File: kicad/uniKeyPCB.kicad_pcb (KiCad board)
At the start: 2 copper layers, 84 x 84 mm, 136 parts, among them J1 Conn_01x03_Socket, J10 Conn_01x02_Socket, J2 Conn_01x03_Socket, J3 Conn_01x02_Socket, J4 Conn_01x02_Socket, J5 Conn_01x03_Socket, J6 Conn_01x03_Socket, J9 Conn_01x02_Socket, SW1 SW_CHOC_HS, SW2 SW_MX_HS

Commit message: wip
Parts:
- removed the D1 at (75.5, 130.6)
- removed the D1 at (118.6, 130.6)
- removed the D1 at (75.5, 87.6)
- removed the D1 at (75.5, 109.1)
- removed the D1 at (118.6, 66.1)
- removed the D1 at (75.5, 66.1)
- removed the D1 at (118.6, 109.0)
- removed the D2 at (85.8, 65.4)
- removed the D2 at (128.8, 129.8)
- removed the D2 at (128.8, 65.4)
- removed the D2 at (85.8, 129.8)
- removed the D2 at (128.8, 108.3)
- removed the D2 at (128.8, 86.9)
- removed the D2 at (85.8, 108.3)
- removed the J1 at (119.2, 54.2)
- removed the J1 at (119.2, 118.6)
- removed the J1 at (76.2, 54.2)
- removed the J1 at (76.2, 75.7)
- removed the J1 at (119.2, 97.1)
- removed the J1 at (76.2, 97.1)
- removed the J1 at (76.2, 118.6)
- removed the J10 at (63.0, 136.0)
- removed the J10 at (106.0, 114.5)
- removed the J10 at (106.0, 71.5)
- removed the J10 at (63.0, 93.0)
- removed the J10 at (63.0, 114.5)
- removed the J10 at (106.0, 135.9)
- removed the J10 at (63.0, 71.5)
- removed the J2 at (76.3, 71.5)
- removed the J2 at (76.3, 114.5)
- removed the J2 at (119.3, 136.0)
- removed the J2 at (76.3, 136.0)
- removed the J2 at (119.3, 71.5)
- removed the J2 at (76.3, 93.0)
- removed the J2 at (119.3, 114.5)
- removed the J3 at (142.1, 71.4)
- removed the J3 at (99.1, 114.4)
- removed the J3 at (142.1, 135.9)
- removed the J3 at (99.1, 135.9)
- removed the J3 at (142.1, 114.4)
- removed the J3 at (99.1, 71.4)
- removed the J3 at (142.1, 92.9)
- removed the J4 at (142.1, 97.3)
- removed the J4 at (142.1, 118.8)
- removed the J4 at (99.1, 54.3)
- removed the J4 at (142.1, 75.8)
- removed the J4 at (99.1, 118.8)
- removed the J4 at (142.1, 54.3)
- removed the J4 at (99.1, 97.3)
- removed the J5 at (128.8, 114.5)
- removed the J5 at (85.8, 71.6)
- removed the J5 at (85.8, 136.0)
- removed the J5 at (85.8, 114.5)
- removed the J5 at (128.8, 136.0)
- removed the J5 at (128.8, 93.0)
- removed the J5 at (128.8, 71.5)
- removed the J6 at (85.9, 118.6)
- removed the J6 at (85.9, 54.1)
- removed the J6 at (128.9, 54.1)
- removed the J6 at (128.9, 118.6)
- removed the J6 at (128.9, 75.6)
- removed the J6 at (128.9, 97.1)
- removed the J6 at (85.9, 97.1)
- removed the J9 at (63.0, 118.8)
- removed the J9 at (106.0, 97.3)
- removed the J9 at (106.0, 54.3)
- removed the J9 at (63.0, 97.3)
- removed the J9 at (63.0, 75.8)
- removed the J9 at (106.0, 118.8)
- removed the J9 at (63.0, 54.3)
- removed the LED1 at (113.3, 122.3)
- removed the LED1 at (70.3, 100.8)
- removed the LED1 at (113.3, 57.8)
- removed the LED1 at (70.3, 79.3)
- removed the LED1 at (113.3, 100.8)
- removed the LED1 at (70.3, 57.8)
- removed the LED1 at (70.3, 122.3)
- removed the LED2 at (134.8, 89.5)
- removed the LED2 at (134.8, 110.9)
- removed the LED2 at (91.8, 110.9)
- removed the LED2 at (91.8, 132.4)
- removed the LED2 at (91.8, 68.0)
- removed the LED2 at (134.8, 68.0)
- removed the LED2 at (134.8, 132.4)
- removed the SW1 at (70.3, 62.9)
- removed the SW1 at (113.3, 127.3)
- removed the SW1 at (113.3, 105.8)
- removed the SW1 at (70.3, 105.9)
- removed the SW1 at (113.3, 62.9)
- removed the SW1 at (70.3, 127.4)
- removed the SW1 at (70.3, 84.4)
- removed the SW2 at (91.8, 62.9)
- removed the SW2 at (134.8, 127.3)
- removed the SW2 at (134.8, 105.8)
- removed the SW2 at (134.8, 62.9)
- removed the SW2 at (91.8, 127.4)
- removed the SW2 at (134.8, 84.4)
- removed the SW2 at (91.8, 105.9)
- removed the mouse-bite-2mm-slot at (113.3, 95.1)
- removed the mouse-bite-2mm-slot at (81.1, 62.9)
- removed the mouse-bite-2mm-slot at (91.8, 95.2)
- removed the mouse-bite-2mm-slot at (70.3, 95.2)
- removed the mouse-bite-2mm-slot at (102.6, 62.9)
- removed the mouse-bite-2mm-slot at (102.6, 127.3)
- removed the mouse-bite-2mm-slot at (102.6, 105.8)
- removed the mouse-bite-2mm-slot at (70.3, 73.7)
- removed the mouse-bite-2mm-slot at (124.1, 127.3)
- removed the mouse-bite-2mm-slot at (124.1, 105.8)
- removed the mouse-bite-2mm-slot at (91.8, 116.6)
- removed the mouse-bite-2mm-slot at (134.8, 73.6)
- removed the mouse-bite-2mm-slot at (113.3, 116.6)
- removed the mouse-bite-2mm-slot at (81.1, 127.4)
- removed the mouse-bite-2mm-slot at (81.1, 84.4)
- removed the mouse-bite-2mm-slot at (134.8, 116.6)
- removed the mouse-bite-2mm-slot at (134.8, 95.1)
- removed the mouse-bite-2mm-slot at (124.1, 62.9)
- removed the mouse-bite-2mm-slot at (81.1, 105.9)
- removed the mouse-bite-2mm-slot at (70.3, 116.6)
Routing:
- net VCC: track 338.8 -> 42.3 mm
- net col0: track 262.1 -> 32.8 mm
- net col1: track 243.6 -> 30.7 mm
- net LED0_out: track 174.1 -> 21.8 mm
- net row1: track 148.0 -> 18.5 mm
- net row0: track 125.2 -> 15.6 mm
- net LED1_in: track 45.0 -> 5.63 mm
- net Net-(D2-A): track 44.6 -> 5.58 mm
- net LED0_in: track 41.0 -> 5.13 mm
- net Net-(D1-A): track 26.6 -> 3.33 mm
- net GND: track 2.11 -> 0.00 mm, vias 16 -> 2
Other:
- board size 84 x 84 mm -> 41 x 19.5 mm
- board text removed: "in"

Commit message: fixed a bug
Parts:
- added D1: 1N4148WS, TB2086_SMD:D3_SMD, F.Cu at (75.6, 66.1)
- added D1: 1N4148WS, TB2086_SMD:D3_SMD, F.Cu at (118.6, 66.1)
- added D1: 1N4148WS, TB2086_SMD:D3_SMD, F.Cu at (75.6, 109.1)
- added D1: 1N4148WS, TB2086_SMD:D3_SMD, F.Cu at (75.6, 87.6)
- added D1: 1N4148WS, TB2086_SMD:D3_SMD, F.Cu at (75.6, 130.6)
- added D1: 1N4148WS, TB2086_SMD:D3_SMD, F.Cu at (118.6, 109.1)
- added D1: 1N4148WS, TB2086_SMD:D3_SMD, F.Cu at (118.6, 130.6)
- added D2: 1N4148WS, TB2086_SMD:D3_SMD, F.Cu at (85.8, 65.4)
- added D2: 1N4148WS, TB2086_SMD:D3_SMD, F.Cu at (85.8, 108.4)
- added D2: 1N4148WS, TB2086_SMD:D3_SMD, F.Cu at (128.8, 65.4)
- added D2: 1N4148WS, TB2086_SMD:D3_SMD, F.Cu at (128.8, 86.9)
- added D2: 1N4148WS, TB2086_SMD:D3_SMD, F.Cu at (128.8, 108.4)
- added D2: 1N4148WS, TB2086_SMD:D3_SMD, F.Cu at (85.8, 129.9)
- added D2: 1N4148WS, TB2086_SMD:D3_SMD, F.Cu at (128.8, 129.9)
- added J1: Conn_01x03_Socket, Connector_PinHeader_2.00mm:PinHeader_1x03_P2.00mm_Vertical, F.Cu at (119.2, 54.2)
- added J1: Conn_01x03_Socket, Connector_PinHeader_2.00mm:PinHeader_1x03_P2.00mm_Vertical, F.Cu at (119.2, 118.7)
- added J1: Conn_01x03_Socket, Connector_PinHeader_2.00mm:PinHeader_1x03_P2.00mm_Vertical, F.Cu at (119.2, 97.2)
- added J1: Conn_01x03_Socket, Connector_PinHeader_2.00mm:PinHeader_1x03_P2.00mm_Vertical, F.Cu at (76.2, 54.2)
- added J1: Conn_01x03_Socket, Connector_PinHeader_2.00mm:PinHeader_1x03_P2.00mm_Vertical, F.Cu at (76.2, 118.7)
- added J1: Conn_01x03_Socket, Connector_PinHeader_2.00mm:PinHeader_1x03_P2.00mm_Vertical, F.Cu at (76.2, 75.7)
- added J1: Conn_01x03_Socket, Connector_PinHeader_2.00mm:PinHeader_1x03_P2.00mm_Vertical, F.Cu at (76.2, 97.2)
- added J10: Conn_01x02_Socket, Connector_PinSocket_2.00mm:PinSocket_1x02_P2.00mm_Vertical, B.Cu at (106.0, 114.5)
- added J10: Conn_01x02_Socket, Connector_PinSocket_2.00mm:PinSocket_1x02_P2.00mm_Vertical, B.Cu at (63.0, 93.0)
- added J10: Conn_01x02_Socket, Connector_PinSocket_2.00mm:PinSocket_1x02_P2.00mm_Vertical, B.Cu at (63.0, 136.0)
- added J10: Conn_01x02_Socket, Connector_PinSocket_2.00mm:PinSocket_1x02_P2.00mm_Vertical, B.Cu at (106.0, 136.0)
- added J10: Conn_01x02_Socket, Connector_PinSocket_2.00mm:PinSocket_1x02_P2.00mm_Vertical, B.Cu at (63.0, 71.5)
- added J10: Conn_01x02_Socket, Connector_PinSocket_2.00mm:PinSocket_1x02_P2.00mm_Vertical, B.Cu at (106.0, 71.5)
- added J10: Conn_01x02_Socket, Connector_PinSocket_2.00mm:PinSocket_1x02_P2.00mm_Vertical, B.Cu at (63.0, 114.5)
- added J2: Conn_01x03_Socket, Connector_PinHeader_2.00mm:PinHeader_1x03_P2.00mm_Vertical, B.Cu at (119.3, 71.5)
- added J2: Conn_01x03_Socket, Connector_PinHeader_2.00mm:PinHeader_1x03_P2.00mm_Vertical, B.Cu at (76.3, 136.0)
- added J2: Conn_01x03_Socket, Connector_PinHeader_2.00mm:PinHeader_1x03_P2.00mm_Vertical, B.Cu at (119.3, 114.5)
- added J2: Conn_01x03_Socket, Connector_PinHeader_2.00mm:PinHeader_1x03_P2.00mm_Vertical, B.Cu at (119.3, 136.0)
- added J2: Conn_01x03_Socket, Connector_PinHeader_2.00mm:PinHeader_1x03_P2.00mm_Vertical, B.Cu at (76.3, 114.5)
- added J2: Conn_01x03_Socket, Connector_PinHeader_2.00mm:PinHeader_1x03_P2.00mm_Vertical, B.Cu at (76.3, 93.0)
- added J2: Conn_01x03_Socket, Connector_PinHeader_2.00mm:PinHeader_1x03_P2.00mm_Vertical, B.Cu at (76.3, 71.5)
- added J3: Conn_01x02_Socket, Connector_PinSocket_2.00mm:PinSocket_1x02_P2.00mm_Vertical, F.Cu at (142.1, 92.9)
- added J3: Conn_01x02_Socket, Connector_PinSocket_2.00mm:PinSocket_1x02_P2.00mm_Vertical, F.Cu at (99.1, 135.9)
- added J3: Conn_01x02_Socket, Connector_PinSocket_2.00mm:PinSocket_1x02_P2.00mm_Vertical, F.Cu at (99.1, 71.4)
- added J3: Conn_01x02_Socket, Connector_PinSocket_2.00mm:PinSocket_1x02_P2.00mm_Vertical, F.Cu at (99.1, 114.4)
- added J3: Conn_01x02_Socket, Connector_PinSocket_2.00mm:PinSocket_1x02_P2.00mm_Vertical, F.Cu at (142.1, 114.4)
- added J3: Conn_01x02_Socket, Connector_PinSocket_2.00mm:PinSocket_1x02_P2.00mm_Vertical, F.Cu at (142.1, 71.4)
- added J3: Conn_01x02_Socket, Connector_PinSocket_2.00mm:PinSocket_1x02_P2.00mm_Vertical, F.Cu at (142.1, 135.9)
- added J4: Conn_01x02_Socket, Connector_PinSocket_2.00mm:PinSocket_1x02_P2.00mm_Vertical, B.Cu at (99.1, 97.3)
- added J4: Conn_01x02_Socket, Connector_PinSocket_2.00mm:PinSocket_1x02_P2.00mm_Vertical, B.Cu at (142.1, 75.8)
- added J4: Conn_01x02_Socket, Connector_PinSocket_2.00mm:PinSocket_1x02_P2.00mm_Vertical, B.Cu at (142.1, 97.3)
- added J4: Conn_01x02_Socket, Connector_PinSocket_2.00mm:PinSocket_1x02_P2.00mm_Vertical, B.Cu at (99.1, 118.8)
- added J4: Conn_01x02_Socket, Connector_PinSocket_2.00mm:PinSocket_1x02_P2.00mm_Vertical, B.Cu at (142.1, 54.3)
- added J4: Conn_01x02_Socket, Connector_PinSocket_2.00mm:PinSocket_1x02_P2.00mm_Vertical, B.Cu at (99.1, 54.3)
- added J4: Conn_01x02_Socket, Connector_PinSocket_2.00mm:PinSocket_1x02_P2.00mm_Vertical, B.Cu at (142.1, 118.8)
- added J5: Conn_01x03_Socket, Connector_PinHeader_2.00mm:PinHeader_1x03_P2.00mm_Vertical, F.Cu at (128.8, 114.6)
- added J5: Conn_01x03_Socket, Connector_PinHeader_2.00mm:PinHeader_1x03_P2.00mm_Vertical, F.Cu at (85.8, 71.6)
- added J5: Conn_01x03_Socket, Connector_PinHeader_2.00mm:PinHeader_1x03_P2.00mm_Vertical, F.Cu at (128.8, 136.1)
- added J5: Conn_01x03_Socket, Connector_PinHeader_2.00mm:PinHeader_1x03_P2.00mm_Vertical, F.Cu at (85.8, 114.6)
- added J5: Conn_01x03_Socket, Connector_PinHeader_2.00mm:PinHeader_1x03_P2.00mm_Vertical, F.Cu at (128.8, 93.1)
- added J5: Conn_01x03_Socket, Connector_PinHeader_2.00mm:PinHeader_1x03_P2.00mm_Vertical, F.Cu at (128.8, 71.6)
- added J5: Conn_01x03_Socket, Connector_PinHeader_2.00mm:PinHeader_1x03_P2.00mm_Vertical, F.Cu at (85.8, 136.1)
- added J6: Conn_01x03_Socket, Connector_PinHeader_2.00mm:PinHeader_1x03_P2.00mm_Vertical, B.Cu at (128.9, 97.1)
- added J6: Conn_01x03_Socket, Connector_PinHeader_2.00mm:PinHeader_1x03_P2.00mm_Vertical, B.Cu at (85.9, 54.1)
- added J6: Conn_01x03_Socket, Connector_PinHeader_2.00mm:PinHeader_1x03_P2.00mm_Vertical, B.Cu at (128.9, 75.6)
- added J6: Conn_01x03_Socket, Connector_PinHeader_2.00mm:PinHeader_1x03_P2.00mm_Vertical, B.Cu at (128.9, 54.1)
- added J6: Conn_01x03_Socket, Connector_PinHeader_2.00mm:PinHeader_1x03_P2.00mm_Vertical, B.Cu at (128.9, 118.6)
- added J6: Conn_01x03_Socket, Connector_PinHeader_2.00mm:PinHeader_1x03_P2.00mm_Vertical, B.Cu at (85.9, 118.6)
- added J6: Conn_01x03_Socket, Connector_PinHeader_2.00mm:PinHeader_1x03_P2.00mm_Vertical, B.Cu at (85.9, 97.1)
- added J9: Conn_01x02_Socket, Connector_PinSocket_2.00mm:PinSocket_1x02_P2.00mm_Vertical, F.Cu at (63.0, 75.8)
- added J9: Conn_01x02_Socket, Connector_PinSocket_2.00mm:PinSocket_1x02_P2.00mm_Vertical, F.Cu at (106.0, 54.3)
- added J9: Conn_01x02_Socket, Connector_PinSocket_2.00mm:PinSocket_1x02_P2.00mm_Vertical, F.Cu at (63.0, 97.3)
- added J9: Conn_01x02_Socket, Connector_PinSocket_2.00mm:PinSocket_1x02_P2.00mm_Vertical, F.Cu at (106.0, 118.8)
- added J9: Conn_01x02_Socket, Connector_PinSocket_2.00mm:PinSocket_1x02_P2.00mm_Vertical, F.Cu at (106.0, 97.3)
- added J9: Conn_01x02_Socket, Connector_PinSocket_2.00mm:PinSocket_1x02_P2.00mm_Vertical, F.Cu at (63.0, 118.8)
- added J9: Conn_01x02_Socket, Connector_PinSocket_2.00mm:PinSocket_1x02_P2.00mm_Vertical, F.Cu at (63.0, 54.3)
- added LED1: SK6812MINI-E, TB2086_LED:LED_SW_SK6812-E-rot, F.Cu at (113.3, 100.8)
- added LED1: SK6812MINI-E, TB2086_LED:LED_SW_SK6812-E-rot, F.Cu at (70.3, 100.8)
- added LED1: SK6812MINI-E, TB2086_LED:LED_SW_SK6812-E-rot, F.Cu at (70.3, 79.3)
- added LED1: SK6812MINI-E, TB2086_LED:LED_SW_SK6812-E-rot, F.Cu at (113.3, 57.8)
- added LED1: SK6812MINI-E, TB2086_LED:LED_SW_SK6812-E-rot, F.Cu at (113.3, 122.3)
- added LED1: SK6812MINI-E, TB2086_LED:LED_SW_SK6812-E-rot, F.Cu at (70.3, 122.3)
- added LED1: SK6812MINI-E, TB2086_LED:LED_SW_SK6812-E-rot, F.Cu at (70.3, 57.8)
- added LED2: SK6812MINI-E, TB2086_LED:LED_SW_SK6812-E-rot, F.Cu at (134.8, 89.5)
- added LED2: SK6812MINI-E, TB2086_LED:LED_SW_SK6812-E-rot, F.Cu at (134.8, 68.0)
- added LED2: SK6812MINI-E, TB2086_LED:LED_SW_SK6812-E-rot, F.Cu at (134.8, 111.0)
- added LED2: SK6812MINI-E, TB2086_LED:LED_SW_SK6812-E-rot, F.Cu at (134.8, 132.5)
- added LED2: SK6812MINI-E, TB2086_LED:LED_SW_SK6812-E-rot, F.Cu at (91.8, 68.0)
- added LED2: SK6812MINI-E, TB2086_LED:LED_SW_SK6812-E-rot, F.Cu at (91.8, 111.0)
- added LED2: SK6812MINI-E, TB2086_LED:LED_SW_SK6812-E-rot, F.Cu at (91.8, 132.5)
- added SW1: SW_CHOC_HS, TB2086_KEYSWITCH:SW_choc_v1_v2_HS_1u, F.Cu at (113.3, 105.9)
- added SW1: SW_CHOC_HS, TB2086_KEYSWITCH:SW_choc_v1_v2_HS_1u, F.Cu at (70.3, 84.4)
- added SW1: SW_CHOC_HS, TB2086_KEYSWITCH:SW_choc_v1_v2_HS_1u, F.Cu at (70.3, 62.9)
- added SW1: SW_CHOC_HS, TB2086_KEYSWITCH:SW_choc_v1_v2_HS_1u, F.Cu at (70.3, 105.9)
- added SW1: SW_CHOC_HS, TB2086_KEYSWITCH:SW_choc_v1_v2_HS_1u, F.Cu at (70.3, 127.4)
- added SW1: SW_CHOC_HS, TB2086_KEYSWITCH:SW_choc_v1_v2_HS_1u, F.Cu at (113.3, 127.4)
- added SW1: SW_CHOC_HS, TB2086_KEYSWITCH:SW_choc_v1_v2_HS_1u, F.Cu at (113.3, 62.9)
- added SW2: SW_MX_HS, TB2086_KEYSWITCH:SW_MX_HS_1u, F.Cu at (91.8, 127.4)
- added SW2: SW_MX_HS, TB2086_KEYSWITCH:SW_MX_HS_1u, F.Cu at (134.8, 62.9)
- added SW2: SW_MX_HS, TB2086_KEYSWITCH:SW_MX_HS_1u, F.Cu at (134.8, 105.9)
- added SW2: SW_MX_HS, TB2086_KEYSWITCH:SW_MX_HS_1u, F.Cu at (134.8, 127.4)
- added SW2: SW_MX_HS, TB2086_KEYSWITCH:SW_MX_HS_1u, F.Cu at (134.8, 84.4)
- added SW2: SW_MX_HS, TB2086_KEYSWITCH:SW_MX_HS_1u, F.Cu at (91.8, 105.9)
- added SW2: SW_MX_HS, TB2086_KEYSWITCH:SW_MX_HS_1u, F.Cu at (91.8, 62.9)
- added mouse-bite-2mm-slot: VAL**, Mouse_Bite:mouse-bite-2mm-slot, F.Cu at (81.1, 84.4)
- added mouse-bite-2mm-slot: VAL**, Mouse_Bite:mouse-bite-2mm-slot, F.Cu at (113.3, 116.6)
- added mouse-bite-2mm-slot: VAL**, Mouse_Bite:mouse-bite-2mm-slot, F.Cu at (91.8, 116.7)
- added mouse-bite-2mm-slot: VAL**, Mouse_Bite:mouse-bite-2mm-slot, F.Cu at (102.6, 62.9)
- added mouse-bite-2mm-slot: VAL**, Mouse_Bite:mouse-bite-2mm-slot, F.Cu at (59.6, 127.4)
- added mouse-bite-2mm-slot: VAL**, Mouse_Bite:mouse-bite-2mm-slot, F.Cu at (124.1, 62.9)
- added mouse-bite-2mm-slot: VAL**, Mouse_Bite:mouse-bite-2mm-slot, F.Cu at (102.6, 105.9)
- added mouse-bite-2mm-slot: VAL**, Mouse_Bite:mouse-bite-2mm-slot, F.Cu at (145.6, 84.4)
- added mouse-bite-2mm-slot: VAL**, Mouse_Bite:mouse-bite-2mm-slot, F.Cu at (145.6, 62.9)
- added mouse-bite-2mm-slot: VAL**, Mouse_Bite:mouse-bite-2mm-slot, F.Cu at (124.1, 127.4)
- added mouse-bite-2mm-slot: VAL**, Mouse_Bite:mouse-bite-2mm-slot, F.Cu at (145.6, 127.4)
- added mouse-bite-2mm-slot: VAL**, Mouse_Bite:mouse-bite-2mm-slot, F.Cu at (81.1, 127.4)
- added mouse-bite-2mm-slot: VAL**, Mouse_Bite:mouse-bite-2mm-slot, F.Cu at (113.3, 138.1)
- added mouse-bite-2mm-slot: VAL**, Mouse_Bite:mouse-bite-2mm-slot, F.Cu at (70.3, 73.6)
- added mouse-bite-2mm-slot: VAL**, Mouse_Bite:mouse-bite-2mm-slot, F.Cu at (134.8, 116.7)
- added mouse-bite-2mm-slot: VAL**, Mouse_Bite:mouse-bite-2mm-slot, F.Cu at (81.1, 62.9)
- added mouse-bite-2mm-slot: VAL**, Mouse_Bite:mouse-bite-2mm-slot, F.Cu at (70.3, 52.1)
- added mouse-bite-2mm-slot: VAL**, Mouse_Bite:mouse-bite-2mm-slot, F.Cu at (134.8, 138.2)
- added mouse-bite-2mm-slot: VAL**, Mouse_Bite:mouse-bite-2mm-slot, F.Cu at (113.3, 52.1)
- added mouse-bite-2mm-slot: VAL**, Mouse_Bite:mouse-bite-2mm-slot, F.Cu at (134.8, 73.7)
- added mouse-bite-2mm-slot: VAL**, Mouse_Bite:mouse-bite-2mm-slot, F.Cu at (113.3, 95.1)
- added mouse-bite-2mm-slot: VAL**, Mouse_Bite:mouse-bite-2mm-slot, F.Cu at (70.3, 138.1)
- added mouse-bite-2mm-slot: VAL**, Mouse_Bite:mouse-bite-2mm-slot, F.Cu at (59.6, 105.9)
- added mouse-bite-2mm-slot: VAL**, Mouse_Bite:mouse-bite-2mm-slot, F.Cu at (59.6, 84.4)
- added mouse-bite-2mm-slot: VAL**, Mouse_Bite:mouse-bite-2mm-slot, F.Cu at (91.8, 138.2)
- added mouse-bite-2mm-slot: VAL**, Mouse_Bite:mouse-bite-2mm-slot, F.Cu at (70.3, 116.6)
- added mouse-bite-2mm-slot: VAL**, Mouse_Bite:mouse-bite-2mm-slot, F.Cu at (145.6, 105.9)
- added mouse-bite-2mm-slot: VAL**, Mouse_Bite:mouse-bite-2mm-slot, F.Cu at (59.6, 62.9)
- added mouse-bite-2mm-slot: VAL**, Mouse_Bite:mouse-bite-2mm-slot, F.Cu at (91.8, 95.2)
- added mouse-bite-2mm-slot: VAL**, Mouse_Bite:mouse-bite-2mm-slot, F.Cu at (134.8, 95.2)
- added mouse-bite-2mm-slot: VAL**, Mouse_Bite:mouse-bite-2mm-slot, F.Cu at (134.8, 52.1)
- added mouse-bite-2mm-slot: VAL**, Mouse_Bite:mouse-bite-2mm-slot, F.Cu at (124.1, 105.9)
- added mouse-bite-2mm-slot: VAL**, Mouse_Bite:mouse-bite-2mm-slot, F.Cu at (102.6, 127.4)
- added mouse-bite-2mm-slot: VAL**, Mouse_Bite:mouse-bite-2mm-slot, F.Cu at (70.3, 95.1)
- added mouse-bite-2mm-slot: VAL**, Mouse_Bite:mouse-bite-2mm-slot, F.Cu at (81.1, 105.9)
- added mouse-bite-2mm-slot: VAL**, Mouse_Bite:mouse-bite-2mm-slot, F.Cu at (91.8, 52.1)
- J10, J2, J4, J6: moved to B.Cu
- turned J10 to 45 degrees
- turned J2 to -45 degrees
- turned J4 to -135 degrees
- turned J6 to 135 degrees
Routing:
- net VCC: track 42.3 -> 338.8 mm
- net col0: track 32.8 -> 262.1 mm
- net col1: track 30.7 -> 223.0 mm
- net LED1_out: track 0.00 -> 155.5 mm
- net LED0_out: track 21.8 -> 174.1 mm
- net row1: track 18.5 -> 148.0 mm
- net row0: track 15.6 -> 125.2 mm
- net LED1_in: track 5.63 -> 45.0 mm
- net Net-(D2-A): track 5.58 -> 44.6 mm
- net LED0_in: track 5.13 -> 41.0 mm
- net Net-(D1-A): track 3.33 -> 26.6 mm
- net GND: vias 2 -> 32
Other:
- board size 41 x 19.5 mm -> 94 x 94 mm
- board text added: "<- VCC ->"
- board text added: "<- row ->"
- board text added: "Whether you're a experienced keyboard builder or a beginner, uniKey provides a convenient solution for creating"
- board text added: "https://github.com/Thunderbird2086/uniKeyPCB"
- board text added: "in"
- board text added: "uniKey: A Compact PCB for Single Key Switches - v0.2.2"
- board text added: "unique and personalized keyboards. Happy building!"
- board text added: "v0.2.2"
- board text removed: "led in"
- board text removed: "row"

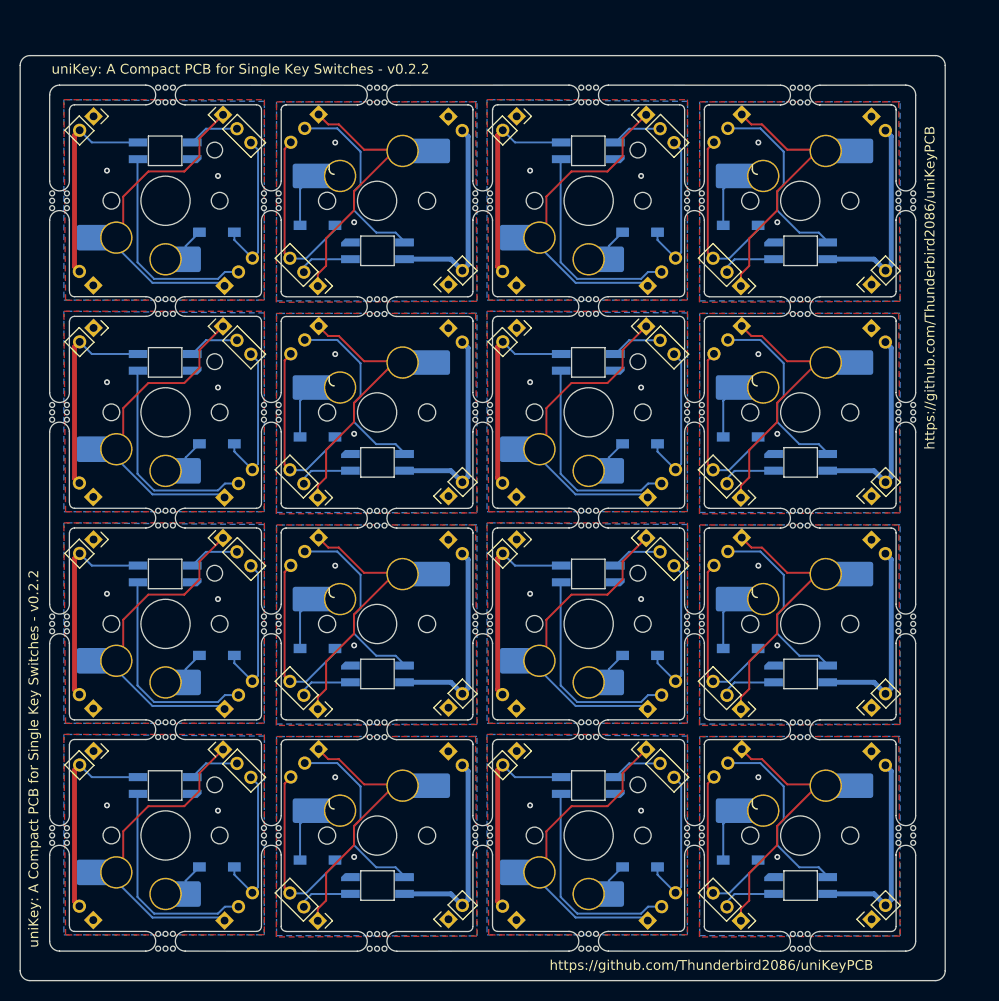
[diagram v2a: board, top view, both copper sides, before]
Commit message: fixed silkscreen
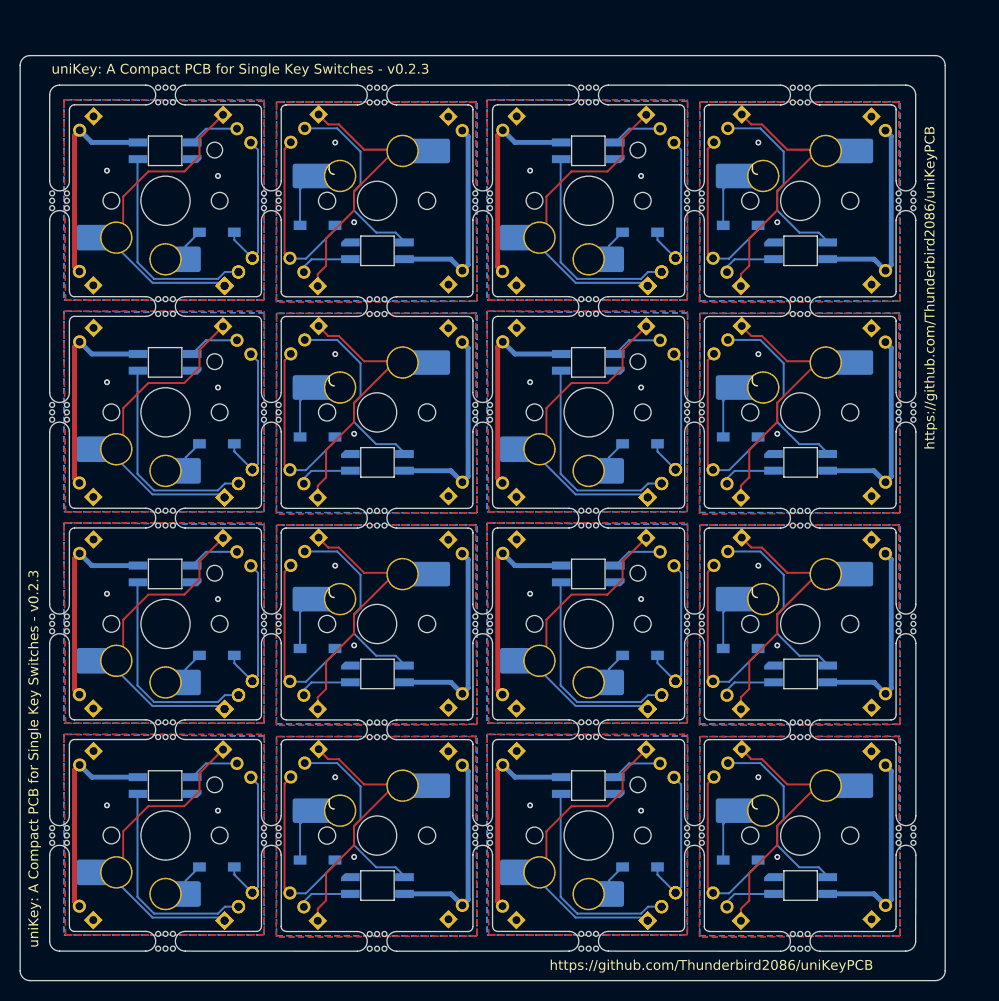
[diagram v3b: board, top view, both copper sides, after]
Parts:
- removed J10 (x7), J9 (x7): Conn_01x02_Socket, Connector_PinSocket_2.00mm:PinSocket_1x02_P2.00mm_Vertical
- removed the J2 at (119.3, 71.5)
- removed the J2 at (76.3, 136.0)
- removed the J2 at (119.3, 114.5)
- removed the J2 at (119.3, 136.0)
- removed the J2 at (76.3, 114.5)
- removed the J2 at (76.3, 93.0)
- removed the J2 at (119.3, 93.0)
- removed the J3 at (142.1, 92.9)
- removed the J3 at (99.1, 92.9)
- removed the J3 at (99.1, 135.9)
- removed the J3 at (99.1, 114.4)
- removed the J3 at (142.1, 114.4)
- removed the J3 at (142.1, 71.4)
- removed the J3 at (142.1, 135.9)
- removed the J4 at (99.1, 97.3)
- removed the J4 at (142.1, 75.8)
- removed the J4 at (142.1, 97.3)
- removed the J4 at (99.1, 118.8)
- removed the J4 at (142.1, 54.3)
- removed the J4 at (99.1, 75.8)
- removed the J4 at (142.1, 118.8)
- removed the J5 at (128.8, 114.6)
- removed the J5 at (85.8, 93.1)
- removed the J5 at (128.8, 136.1)
- removed the J5 at (85.8, 114.6)
- removed the J5 at (128.8, 93.1)
- removed the J5 at (128.8, 71.6)
- removed the J5 at (85.8, 136.1)
- removed the J6 at (128.9, 97.1)
- removed the J6 at (85.9, 75.6)
- removed the J6 at (128.9, 75.6)
- removed the J6 at (128.9, 54.1)
- removed the J6 at (128.9, 118.6)
- removed the J6 at (85.9, 118.6)
- removed the J6 at (85.9, 97.1)
- removed the mouse-bite-2mm-slot at (145.6, 84.4)
- removed the mouse-bite-2mm-slot at (145.6, 62.9)
- removed the mouse-bite-2mm-slot at (145.6, 127.4)
- removed the mouse-bite-2mm-slot at (145.6, 105.9)
- added J2 (x2): Conn_01x03_Socket, Connector_PinHeader_2.00mm:PinHeader_1x03_P2.00mm_Vertical, B.Cu at (76.3, 136.0)
- added J2 (x2): Conn_01x03_Socket, Connector_PinHeader_2.00mm:PinHeader_1x03_P2.00mm_Vertical, B.Cu at (119.3, 71.5)
- added J2 (x2): Conn_01x03_Socket, Connector_PinHeader_2.00mm:PinHeader_1x03_P2.00mm_Vertical, B.Cu at (119.3, 114.5)
- added J2 (x2): Conn_01x03_Socket, Connector_PinHeader_2.00mm:PinHeader_1x03_P2.00mm_Vertical, B.Cu at (76.3, 114.5)
- added J2 (x2): Conn_01x03_Socket, Connector_PinHeader_2.00mm:PinHeader_1x03_P2.00mm_Vertical, B.Cu at (119.3, 136.0)
- added J2 (x2): Conn_01x03_Socket, Connector_PinHeader_2.00mm:PinHeader_1x03_P2.00mm_Vertical, B.Cu at (76.3, 93.0)
- added J2: Conn_01x03_Socket, Connector_PinHeader_2.00mm:PinHeader_1x03_P2.00mm_Vertical, B.Cu at (76.3, 71.5)
- added J2 (x2): Conn_01x03_Socket, Connector_PinHeader_2.00mm:PinHeader_1x03_P2.00mm_Vertical, B.Cu at (119.3, 93.0)
- added J3: Conn_01x03_Socket, Connector_PinHeader_2.00mm:PinHeader_1x03_P2.00mm_Vertical, B.Cu at (128.8, 71.6)
- added J3: Conn_01x03_Socket, Connector_PinHeader_2.00mm:PinHeader_1x03_P2.00mm_Vertical, B.Cu at (128.8, 136.1)
- added J3: Conn_01x03_Socket, Connector_PinHeader_2.00mm:PinHeader_1x03_P2.00mm_Vertical, B.Cu at (128.8, 114.6)
- added J3: Conn_01x03_Socket, Connector_PinHeader_2.00mm:PinHeader_1x03_P2.00mm_Vertical, B.Cu at (85.8, 136.1)
- added J3: Conn_01x03_Socket, Connector_PinHeader_2.00mm:PinHeader_1x03_P2.00mm_Vertical, B.Cu at (128.8, 93.1)
- added J3: Conn_01x03_Socket, Connector_PinHeader_2.00mm:PinHeader_1x03_P2.00mm_Vertical, B.Cu at (85.8, 93.1)
- added J3: Conn_01x03_Socket, Connector_PinHeader_2.00mm:PinHeader_1x03_P2.00mm_Vertical, B.Cu at (85.8, 114.6)
- added J4: Conn_01x03_Socket, Connector_PinHeader_2.00mm:PinHeader_1x03_P2.00mm_Vertical, B.Cu at (85.9, 75.6)
- added J4: Conn_01x03_Socket, Connector_PinHeader_2.00mm:PinHeader_1x03_P2.00mm_Vertical, B.Cu at (85.9, 118.6)
- added J4: Conn_01x03_Socket, Connector_PinHeader_2.00mm:PinHeader_1x03_P2.00mm_Vertical, B.Cu at (128.9, 118.6)
- added J4: Conn_01x03_Socket, Connector_PinHeader_2.00mm:PinHeader_1x03_P2.00mm_Vertical, B.Cu at (128.9, 75.6)
- added J4: Conn_01x03_Socket, Connector_PinHeader_2.00mm:PinHeader_1x03_P2.00mm_Vertical, B.Cu at (85.9, 97.1)
- added J4: Conn_01x03_Socket, Connector_PinHeader_2.00mm:PinHeader_1x03_P2.00mm_Vertical, B.Cu at (128.9, 97.1)
- added J4: Conn_01x03_Socket, Connector_PinHeader_2.00mm:PinHeader_1x03_P2.00mm_Vertical, B.Cu at (128.9, 54.1)
- added J5: Conn_01x02_Socket, Connector_PinSocket_2.00mm:PinSocket_1x02_P2.00mm_Vertical, B.Cu at (106.0, 118.8)
- added J5: Conn_01x02_Socket, Connector_PinSocket_2.00mm:PinSocket_1x02_P2.00mm_Vertical, B.Cu at (63.0, 118.8)
- added J5: Conn_01x02_Socket, Connector_PinSocket_2.00mm:PinSocket_1x02_P2.00mm_Vertical, B.Cu at (106.0, 75.8)
- added J5: Conn_01x02_Socket, Connector_PinSocket_2.00mm:PinSocket_1x02_P2.00mm_Vertical, B.Cu at (63.0, 75.8)
- added J5: Conn_01x02_Socket, Connector_PinSocket_2.00mm:PinSocket_1x02_P2.00mm_Vertical, B.Cu at (63.0, 97.3)
- added J5: Conn_01x02_Socket, Connector_PinSocket_2.00mm:PinSocket_1x02_P2.00mm_Vertical, B.Cu at (106.0, 97.3)
- added J5: Conn_01x02_Socket, Connector_PinSocket_2.00mm:PinSocket_1x02_P2.00mm_Vertical, B.Cu at (106.0, 54.3)
- added J6: Conn_01x02_Socket, Connector_PinSocket_2.00mm:PinSocket_1x02_P2.00mm_Vertical, B.Cu at (142.1, 135.9)
- added J6: Conn_01x02_Socket, Connector_PinSocket_2.00mm:PinSocket_1x02_P2.00mm_Vertical, B.Cu at (142.1, 92.9)
- added J6: Conn_01x02_Socket, Connector_PinSocket_2.00mm:PinSocket_1x02_P2.00mm_Vertical, B.Cu at (99.1, 92.9)
- added J6: Conn_01x02_Socket, Connector_PinSocket_2.00mm:PinSocket_1x02_P2.00mm_Vertical, B.Cu at (99.1, 135.9)
- added J6: Conn_01x02_Socket, Connector_PinSocket_2.00mm:PinSocket_1x02_P2.00mm_Vertical, B.Cu at (99.1, 114.4)
- added J6: Conn_01x02_Socket, Connector_PinSocket_2.00mm:PinSocket_1x02_P2.00mm_Vertical, B.Cu at (142.1, 71.4)
- added J6: Conn_01x02_Socket, Connector_PinSocket_2.00mm:PinSocket_1x02_P2.00mm_Vertical, B.Cu at (142.1, 114.4)
- added J7: Conn_01x02_Socket, Connector_PinSocket_2.00mm:PinSocket_1x02_P2.00mm_Vertical, B.Cu at (63.0, 136.0)
- added J7: Conn_01x02_Socket, Connector_PinSocket_2.00mm:PinSocket_1x02_P2.00mm_Vertical, B.Cu at (106.0, 114.5)
- added J7: Conn_01x02_Socket, Connector_PinSocket_2.00mm:PinSocket_1x02_P2.00mm_Vertical, B.Cu at (63.0, 114.5)
- added J7: Conn_01x02_Socket, Connector_PinSocket_2.00mm:PinSocket_1x02_P2.00mm_Vertical, B.Cu at (63.0, 93.0)
- added J7: Conn_01x02_Socket, Connector_PinSocket_2.00mm:PinSocket_1x02_P2.00mm_Vertical, B.Cu at (106.0, 93.0)
- added J7: Conn_01x02_Socket, Connector_PinSocket_2.00mm:PinSocket_1x02_P2.00mm_Vertical, B.Cu at (106.0, 71.5)
- added J7: Conn_01x02_Socket, Connector_PinSocket_2.00mm:PinSocket_1x02_P2.00mm_Vertical, B.Cu at (106.0, 136.0)
- added J8: Conn_01x02_Socket, Connector_PinSocket_2.00mm:PinSocket_1x02_P2.00mm_Vertical, B.Cu at (99.1, 118.8)
- added J8: Conn_01x02_Socket, Connector_PinSocket_2.00mm:PinSocket_1x02_P2.00mm_Vertical, B.Cu at (142.1, 75.8)
- added J8: Conn_01x02_Socket, Connector_PinSocket_2.00mm:PinSocket_1x02_P2.00mm_Vertical, B.Cu at (99.1, 75.8)
- added J8: Conn_01x02_Socket, Connector_PinSocket_2.00mm:PinSocket_1x02_P2.00mm_Vertical, B.Cu at (142.1, 54.3)
- added J8: Conn_01x02_Socket, Connector_PinSocket_2.00mm:PinSocket_1x02_P2.00mm_Vertical, B.Cu at (99.1, 97.3)
- added J8: Conn_01x02_Socket, Connector_PinSocket_2.00mm:PinSocket_1x02_P2.00mm_Vertical, B.Cu at (142.1, 118.8)
- added J8: Conn_01x02_Socket, Connector_PinSocket_2.00mm:PinSocket_1x02_P2.00mm_Vertical, B.Cu at (142.1, 97.3)
- added mouse-bite-2mm-slot: VAL**, Mouse_Bite:mouse-bite-2mm-slot, F.Cu at (145.6, 105.9)
- added mouse-bite-2mm-slot: VAL**, Mouse_Bite:mouse-bite-2mm-slot, F.Cu at (145.6, 84.4)
- added mouse-bite-2mm-slot: VAL**, Mouse_Bite:mouse-bite-2mm-slot, F.Cu at (145.6, 62.9)
- added mouse-bite-2mm-slot: VAL**, Mouse_Bite:mouse-bite-2mm-slot, F.Cu at (145.6, 127.4)
- J1 (x8): moved to B.Cu
- J3: renamed from J5; moved to B.Cu
- J5: renamed from J9; moved to B.Cu
- J6: renamed from J3; moved to B.Cu
- turned J1 to -135 degrees (x8)
- turned J3 to 45 degrees
- turned J5 to 135 degrees
- turned J6 to -45 degrees
- renumbered J6 to J4, J10 to J7, J4 to J8
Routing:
- net col0: track 262.1 -> 242.3 mm
- net col1: track 223.0 -> 214.9 mm
- net LED1_in: track 45.0 -> 40.3 mm
- net LED1_out: track 155.5 -> 154.7 mm
- net LED0_out: track 174.1 -> 173.4 mm
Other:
- board text added: "uniKey: A Compact PCB for Single Key Switches - v0.2.3"
- board text added: "v0.2.3"
- board text removed: "uniKey: A Compact PCB for Single Key Switches - v0.2.2"
- board text removed: "v0.2.2"
